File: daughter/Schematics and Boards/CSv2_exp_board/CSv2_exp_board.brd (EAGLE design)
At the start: 38.1 x 43.8 mm, 100 parts, among them J1 HIROSE-DF40_44-PIN_CONNECTORS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, J2 J-SERIAL-PORT, J3 CORTEX_DEBUG_SMD, J301 HIROSE-DF40_44-PIN_CONNECTORS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, J7 J-USB-HIROSE-MICRO-USB, SW1 SPST_TACT-KMR2, SW2 SPST_TACT-KMR2, U1 LOADSWITCH-MIC94164, U10 LOADSWITCH-MIC94164, U11 BMI160, U2 ADA4841-1YRJZ-R7, U205 MPL3115A2, U3 Value, U4 RFM69HCW, U5 Value, U6 Value, U7 LOADSWITCH-MIC94164, U8 LOADSWITCH-MIC94164, U9 LOADSWITCH-MIC94164, X1 32.768kHz, X2 32.768, X4 uFL

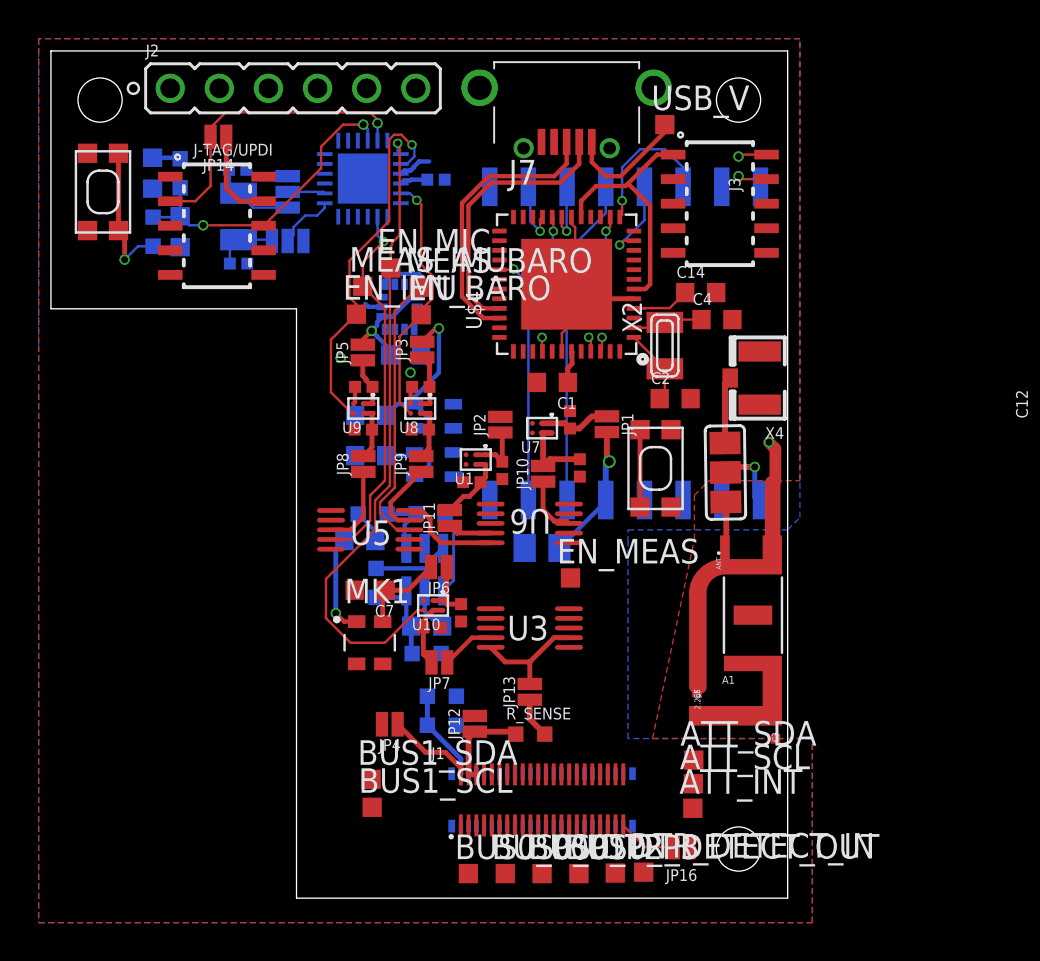
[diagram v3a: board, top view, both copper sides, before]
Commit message: DTR-routing 100% + DRC resolved
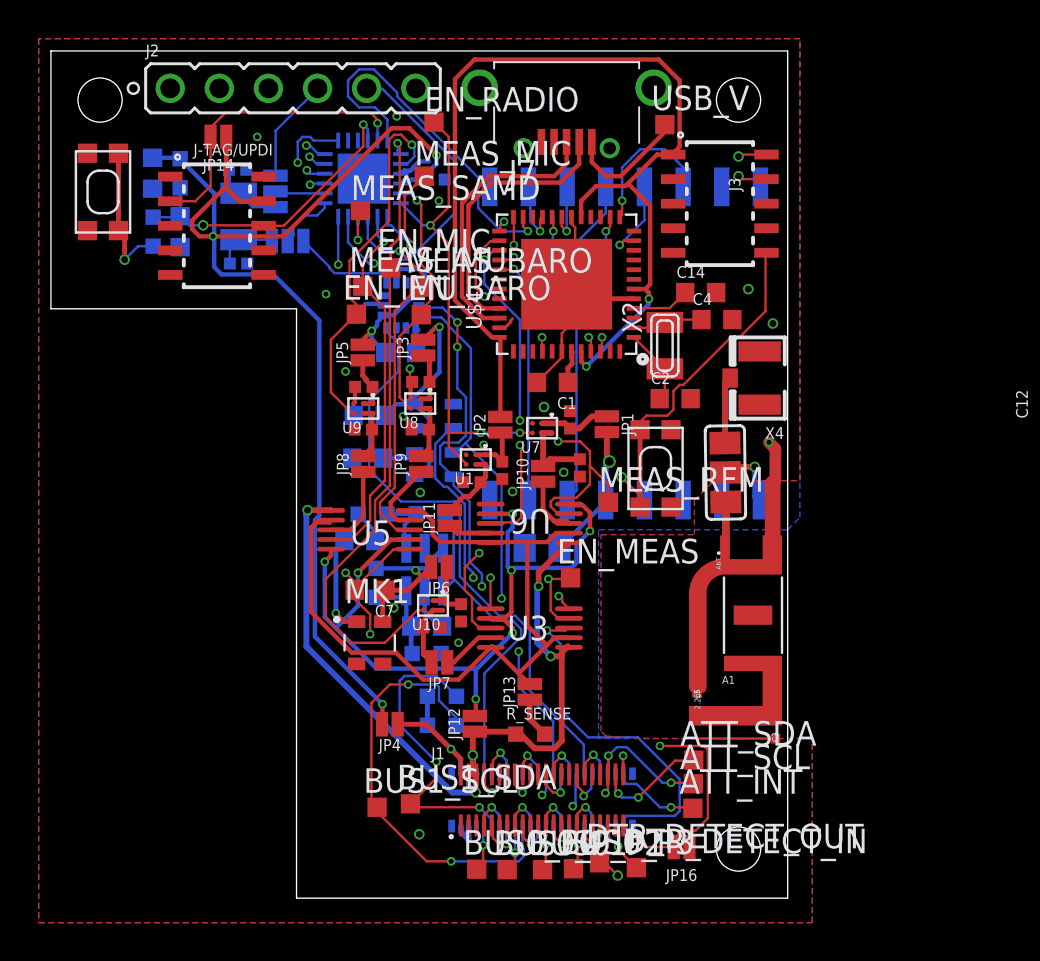
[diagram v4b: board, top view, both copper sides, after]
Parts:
- added EN_RADIO, MEAS_MIC, MEAS_RFM, MEAS_SAMD: TPTP10SQ, TestPoints:TP10SQ
- moved BUS1_SDA 2.40 mm to (18.6, 4.88)
- moved DTR_DETECT_OUT 0.97 mm to (28.4, 1.83)
- moved SJ2 0.64 mm to (11.6, 36.6)
- moved BUS0_P0 0.49 mm to (22.0, 1.50)
- moved DTR_DETECT_IN 0.44 mm to (30.3, 1.57)
- moved BUS0_P3 0.38 mm to (27.0, 1.52)
- moved C25 0.28 mm to (18.1, 28.2)
- moved BUS1_SCL 0.25 mm to (16.9, 4.70)
- moved U8 0.25 mm to (19.1, 25.6)
- moved C20 0.25 mm to (19.1, 26.7)
- moved BUS0_P1 0.23 mm to (23.6, 1.47)
- moved BUS0_P2 0.20 mm to (25.4, 1.47)
- moved C204 0.20 mm to (16.4, 22.8)
- moved JP3 0.11 mm to (19.3, 28.5)
- moved U11 0.11 mm to (18.1, 30.7)
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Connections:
- net EN_RADIO: now also EN_RADIO.TP
- net MEAS_MIC: now also MEAS_MIC.TP
- net MEAS_RFM: now also MEAS_RFM.TP
- net MEAS_SAMD: now also MEAS_SAMD.TP
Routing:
- net BUS0_GPIO0: track 0.00 -> 67.5 mm, vias 0 -> 3
- net +3V3_ATT: track 7.75 -> 63.2 mm, vias 0 -> 3
- net DTR_DETECT_OUT: track 0.00 -> 54.1 mm, vias 0 -> 2
- net DTR_DETECT_IN: track 0.00 -> 52.0 mm, vias 0 -> 2
- net BUS0_SERCOM_P0: track 0.00 -> 50.8 mm, vias 0 -> 2
- net MASTER_I2C_SCL: track 0.00 -> 50.4 mm, vias 0 -> 4
- net MASTER_I2C_SDA: track 0.00 -> 47.8 mm, vias 0 -> 3
- net BUS1_SERCOM_P1: track 0.00 -> 47.3 mm, vias 0 -> 5
- net ATT_INT: track 0.00 -> 45.9 mm, vias 0 -> 3
- net BUS0_GPIO1: track 0.00 -> 44.2 mm, vias 0 -> 2
- net BUS1_SERCOM_P0: track 0.00 -> 44.2 mm, vias 0 -> 3
- net BUS0_SERCOM_P2: track 0.00 -> 44.1 mm, vias 0 -> 3
- net BUS0_SERCOM_P1: track 0.00 -> 43.4 mm, vias 0 -> 2
- net BUS0_SERCOM_P3: track 0.00 -> 42.5 mm, vias 0 -> 2
- net +3V3_SAMD: track 13.2 -> 54.6 mm, vias 0 -> 2
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- added copper zone on layer 15, net GND
- added copper zone on layer 2, net GND

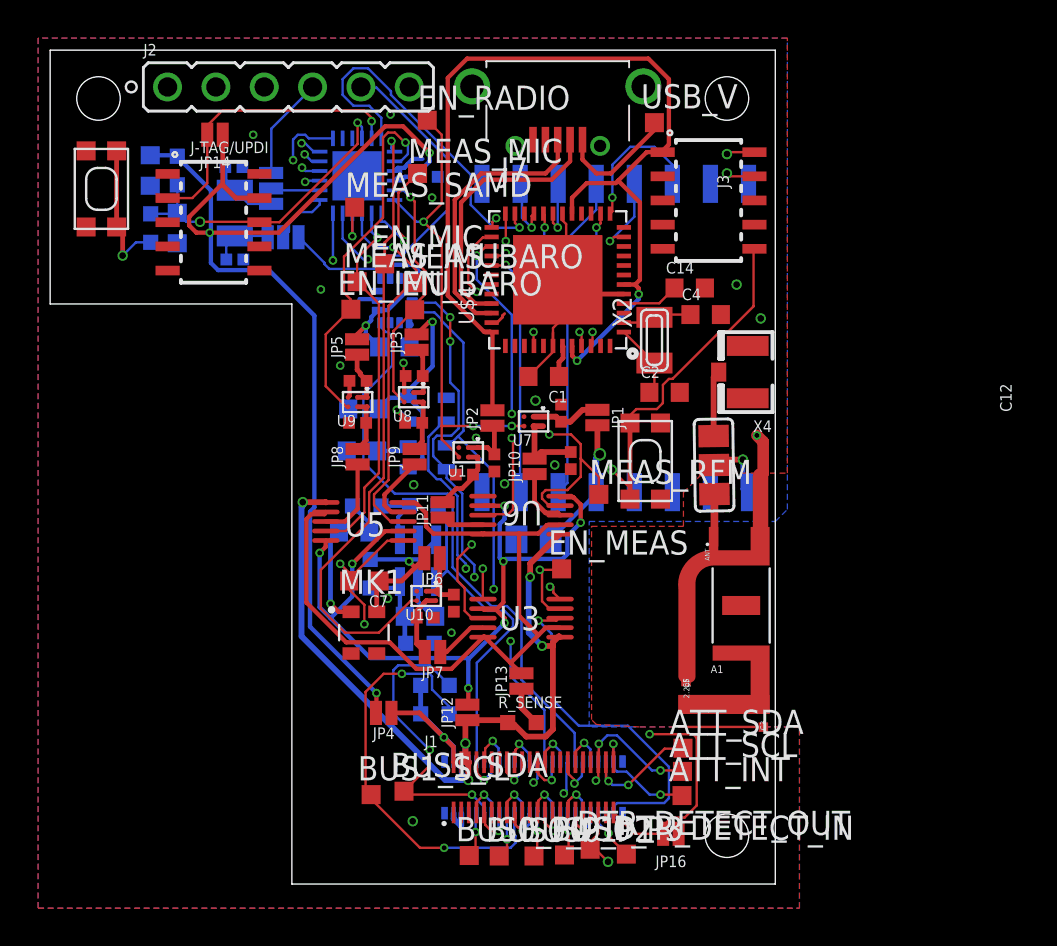
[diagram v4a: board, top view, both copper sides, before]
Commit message: DTR-added text/labels
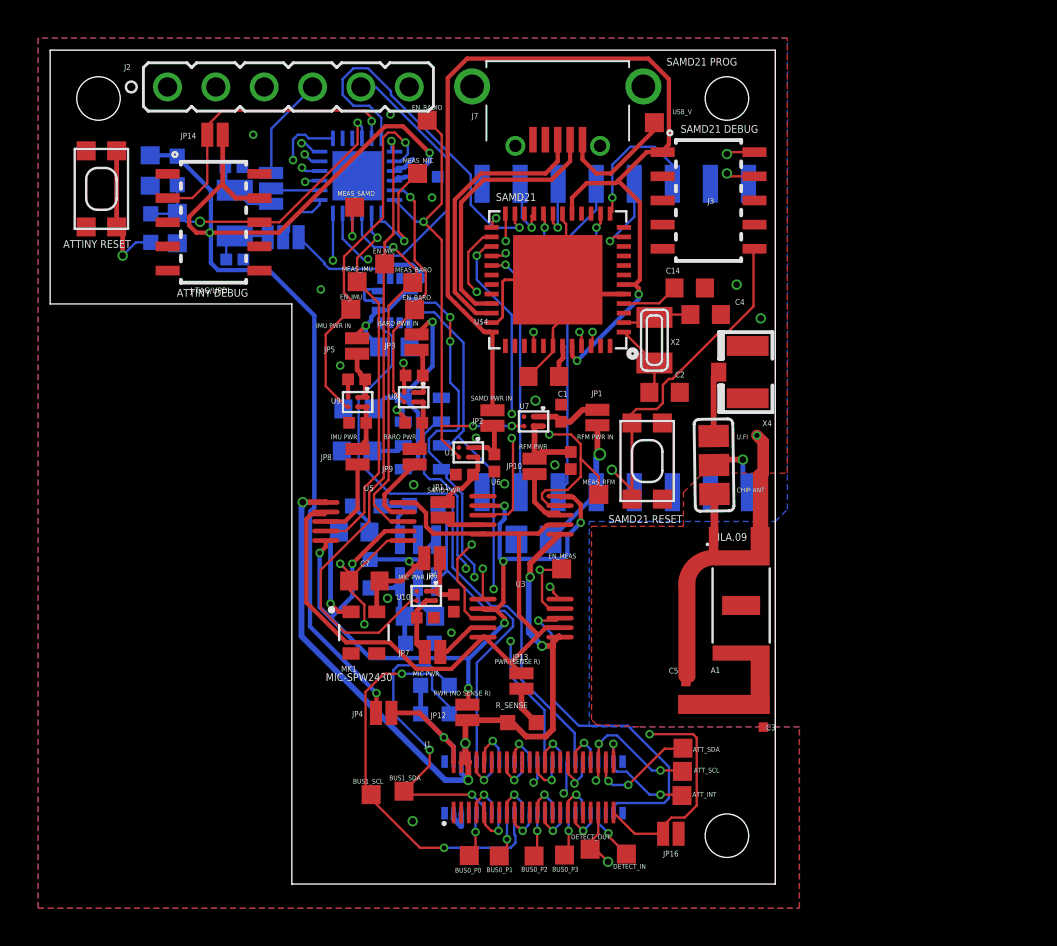
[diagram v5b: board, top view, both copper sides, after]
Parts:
- moved U205 0.25 mm to (19.6, 23.7)
- moved C203 0.25 mm to (16.2, 25.0)
- moved C204 0.25 mm to (16.1, 22.8)
- moved C22 0.11 mm to (16.1, 26.5)
- moved SW2 0.10 mm to (31.4, 22.2)
- moved JP5 0.05 mm to (16.1, 28.3)
- renumbered DTR_DETECT_IN to DETECT_IN, DTR_DETECT_OUT to DETECT_OUT
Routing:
- net GND: track 66.2 -> 62.3 mm
- net BUS1_SERCOM_P1: track 47.3 -> 47.9 mm
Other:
- board text added: "ATTINY DEBUG"
- board text added: "ATTINY RESET"
- board text added: "ATTINY-817"
- board text added: "BARO PWR"
- board text added: "BARO PWR IN"
- board text added: "CHIP ANT"
- board text added: "ILA.09"
- board text added: "IMU PWR"
- board text added: "IMU PWR IN"
- board text added: "IMU-BMI160"
- board text added: "MIC PWR"
- board text added: "MIC PWR IN"
- board text added: "MIC-SPW2430"
- board text added: "MPL3115"
- board text added: "PWR (NO SENSE R)"
- board text added: "PWR (SENSE R)"
- board text added: "RFM PWR"
- board text added: "RFM PWR IN"
- board text added: "SAMD PWR"
- board text added: "SAMD PWR IN"
- board text added: "SAMD21"
- board text added: "SAMD21 DEBUG"
- board text added: "SAMD21 PROG"
- board text added: "SAMD21 RESET"
- board text added: "U.Fl"

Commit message: DTR-added three ufl connectors for rf calibratiion
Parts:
- added R7: (no value), Resistors:R0603
- added X3, X5, X6: uFL, Connectors:U.FL
- moved SW1 1.02 mm to (2.69, 35.5)
- moved J3 0.51 mm to (34.6, 35.4)
- moved JP16 0.49 mm to (32.1, 2.59)
- moved ATT_INT 0.33 mm to (32.9, 4.85)
- moved ATT_SDA 0.30 mm to (32.9, 7.14)
- moved ATT_SCL 0.29 mm to (32.9, 5.99)
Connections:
- new net N$11: R7.1, X6.3
- net GND: now also R7.2, X3.1, X3.2, X5.1, X5.2, X5.3, X6.1, X6.2
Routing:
- net GND: track 62.3 -> 71.0 mm
- net N$11: track 0.00 -> 3.52 mm
- net LORA_RST: track 7.55 -> 6.69 mm
- net N$12: track 8.18 -> 7.46 mm
- net LORA_SCK: track 6.26 -> 5.61 mm
- net SAMD_!RESET: track 28.6 -> 28.1 mm
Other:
- outline, holes or cut-outs redrawn

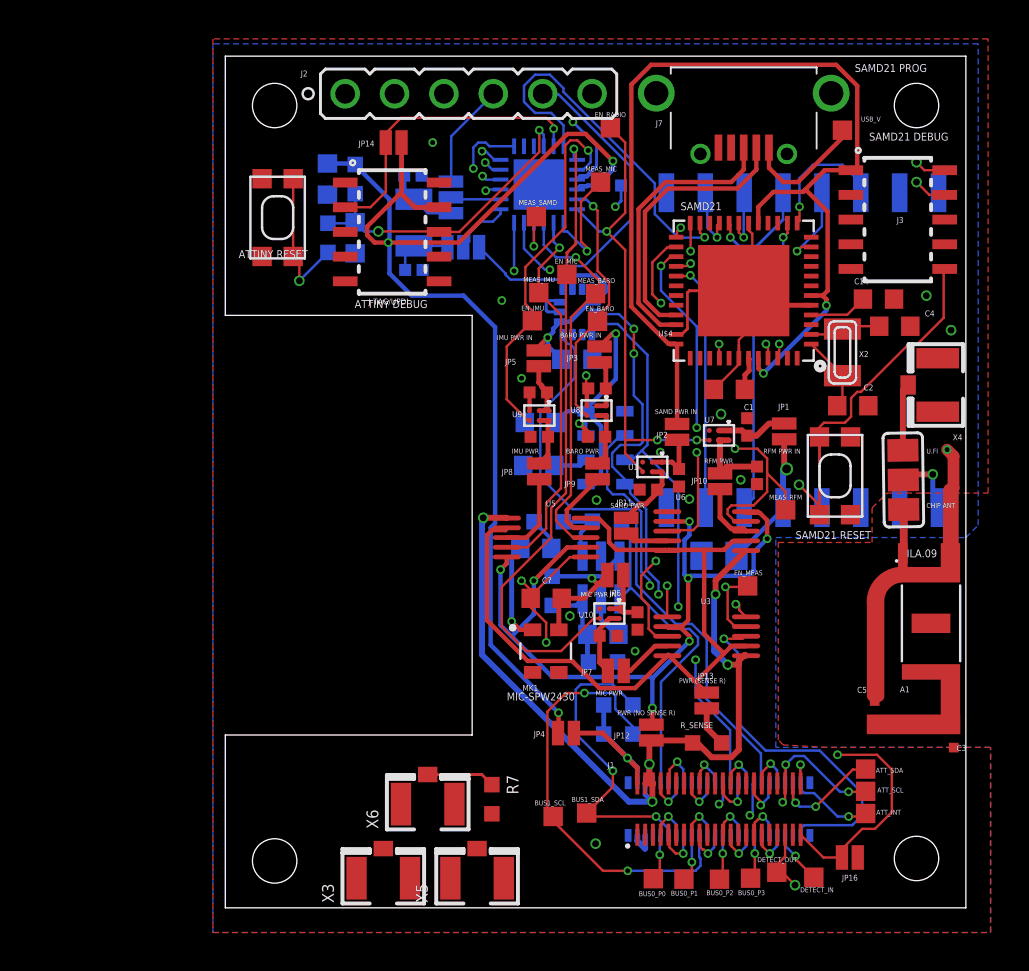
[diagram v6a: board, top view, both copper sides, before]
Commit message: DTR-added codec datasheet and did replacement
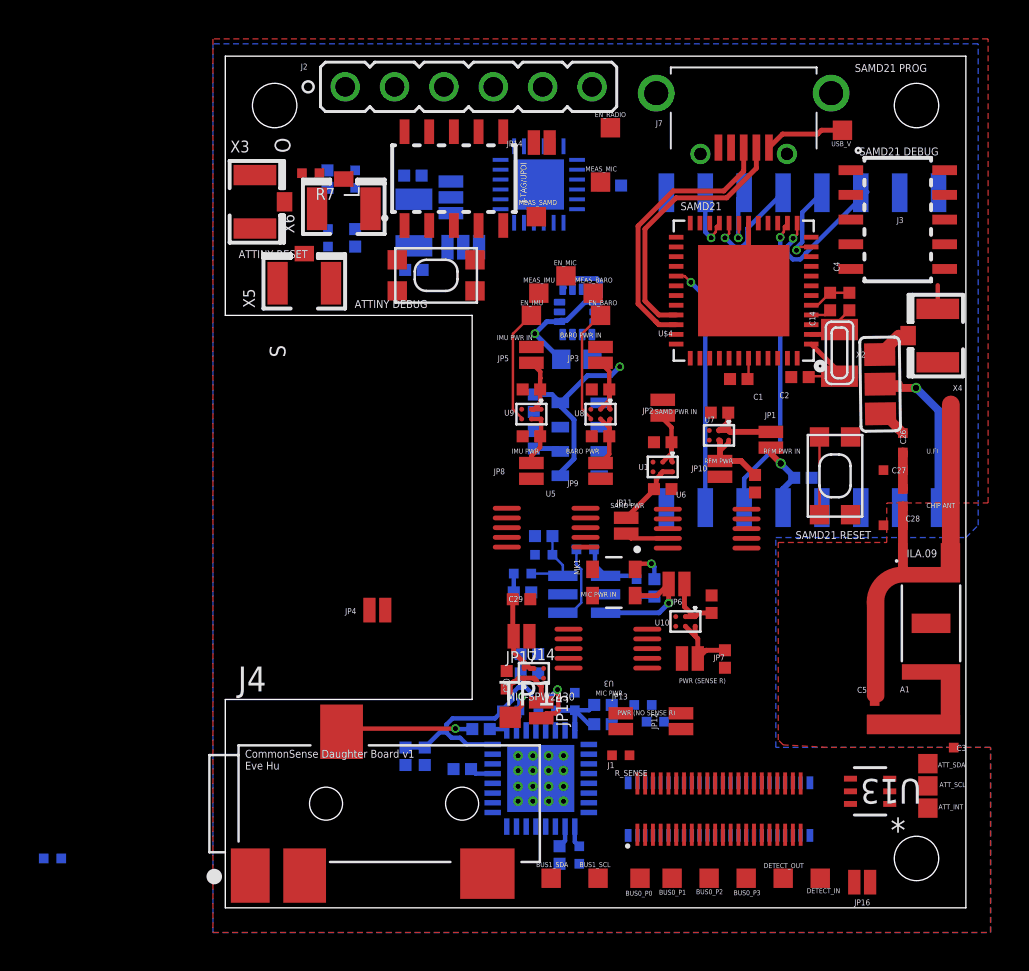
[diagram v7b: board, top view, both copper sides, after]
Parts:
- removed EN_MEAS, MEAS_RFM: TPTP10SQ, TestPoints:TP10SQ
- added C26, C27, C28: (no value), CommonSense-DTR-v1:C0402-S
- added C29: 1u, Capacitors:C0402
- added C30: 100n, Capacitors:C0402
- added C31, C32, C33: (no value), Capacitors:C0402
- added C34, C36, C38: 0.1u, Capacitors:C0402
- added C35, C37, C39: 10u, Capacitors:C0402
- added J4: SJ-43514-SMT, CommonSense-DTR-v1:CUI_SJ-43514-SMT
- added JP15, JP17: JUMPER-SMT_2_NC_PASTELG_NO-SILK, Connectors:SMT-JUMPER_2_NC_PASTE_NO-SILK
- added L1: L0402, Inductors:L0402
- added R10, R11, R9: 100k, Resistors:R0402
- added R12, R8: (no value), Resistors:R0402
- added TP1: TPTP11SQ, TestPoints:TP11SQ
- added U12: TLV320DAC26IRHB, CommonSense-DTR-v1:RHB32_3P45X3P45
- added U13: ADG839YKSZ-500RL7KS_6_ADI-L, CommonSense-DTR-v1:KS_6_ADI-L
- added U14: LOADSWITCH-MIC94164, Switches:WLCSP6_2X3
- C1, C12, C14, C2, C203, C204, C3-4.7N, C4, C6, C7, C8: device Capacitors:C0603 -> Capacitors:C0402
- C9: device Capacitors:C0805 -> Capacitors:C0402
- R1, R1-100K, R2, R3, R3-39R, R4, R5, R6, R7, R_SENSE: device Resistors:R0603 -> Resistors:R0402
- moved X3 35.4 mm to (1.52, 36.3), turned to 0 degrees
- moved R7 33.5 mm to (4.39, 37.8), turned to 180 degrees
- moved X5 31.9 mm to (4.06, 32.1)
- moved X6 30.9 mm to (6.10, 36.0)
- moved JP4 11.6 mm to (7.82, 15.3)
- moved SW1 8.68 mm to (10.8, 32.5), turned to 180 degrees
- moved JP14 7.62 mm to (16.3, 39.4)
- moved C6 6.43 mm to (22.1, 16.5), turned to 270 degrees
- moved R3 6.30 mm to (16.4, 18.2), turned to 0 degrees
- moved C23 6.11 mm to (25.7, 12.8), turned to 270 degrees
- moved C8 5.90 mm to (16.4, 19.1), turned to 0 degrees
- moved C9 5.89 mm to (29.7, 22.1), turned to 180 degrees
- moved R1 5.66 mm to (21.2, 16.5), turned to 270 degrees
- moved U3 5.12 mm to (19.7, 13.3), turned to 0 degrees
- moved SJ3 5.07 mm to (33.7, 26.9)
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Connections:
- new net +3V3_CODEC: C34.1, C35.1, C36.1, C37.1, JP15.2, R11.2, R9.2, U12.2, U12.20, U12.24
- new net +3V3_CODEC_IN: C29.1, JP17.2, U14.A2, U14.B2
- new net +3V3_CODEC_OUT: C30.1, JP15.1, U14.A1, U14.B1
- new net +3V3_CODEC_PWR: JP17.1, U3.3
- new net AGND: C31.2, C36.2, C37.2, J4.2, J4.4, R12.1, U12.15, U12.22
- new net CODEC_!RESET: R11.1, TP1.TP, U12.26
- new net EN_CODEC: ATTINY-817.21, U14.C2
- new net MEAS_CODEC: ATTINY-817.20, U3.4
- new net N$13: C26.2, C27.1, L1.1
- new net N$14: R8.1, U12.9
- new net N$15: C31.1, U12.21
- new net N$16: C32.2, J4.3
- new net N$21: C38.1, C39.1, R10.1, R9.1, U12.32
- new net N$25: C32.1, U12.25
- new net N$27: C33.1, U12.10
- new net N$28: C33.2, J4.1, R8.2
- new net N$9: C26.1, SJ3.1
- new net VGND: U12.23
- net +3V3_DTR: now also U13.2
- net +3V3_MEAS: now also U13.6
- net +3V3_NMEAS: now also U3.5
- net BUS0_AIN0: now also ATTINY-817.24; no longer R2.1, U2.1
- net BUS0_GPIO0: now also U$4.24; no longer ATTINY-817.24, U$4.23
- net BUS0_GPIO1: now also U12.7; no longer U$4.24
- net BUS0_SERCOM_P0: now also U12.5
- net BUS0_SERCOM_P1: now also U12.4
- net BUS0_SERCOM_P3: now also U12.6
- net BUS1_AIN0: now also R2.1, U2.1
- net EN_MEAS: now also U13.1; no longer EN_MEAS.TP, U3.4
- net GND: now also C27.2, C28.1, C28.2, C29.2, C30.2, C34.2, C35.2, C38.2, C39.2, L1.2, R10.2, R12.2, U12.1, U13.3, U14.C1; no longer SJ3.1
- net MEAS_RFM: no longer MEAS_RFM.TP
- net V_SENSE_IN: now also U13.4; no longer U3.5
- net V_SENSE_OUT: now also U13.5; no longer U3.3
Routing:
- net BUS0_GPIO0: track 67.5 -> 0.00 mm, vias 3 -> 0
- net +3V3_ATT: track 63.2 -> 0.00 mm, vias 3 -> 0
- net +3V3_SAMD: track 55.1 -> 0.00 mm, vias 2 -> 0
- net DTR_DETECT_OUT: track 54.1 -> 0.00 mm, vias 2 -> 0
- net DTR_DETECT_IN: track 52.0 -> 0.00 mm, vias 2 -> 0
- net BUS0_SERCOM_P0: track 50.8 -> 0.00 mm, vias 2 -> 0
- net MASTER_I2C_SCL: track 50.1 -> 0.00 mm, vias 4 -> 0
- net BUS1_SERCOM_P1: track 47.9 -> 0.00 mm, vias 5 -> 0
- net MASTER_I2C_SDA: track 47.5 -> 0.00 mm, vias 3 -> 0
- net ATT_INT: track 45.7 -> 0.00 mm, vias 3 -> 0
- net GND: track 71.0 -> 26.5 mm, vias 20 -> 0
- net BUS1_SERCOM_P0: track 44.4 -> 0.00 mm, vias 3 -> 0
- net BUS0_GPIO1: track 44.2 -> 0.00 mm, vias 2 -> 0
- net BUS0_SERCOM_P2: track 44.1 -> 0.00 mm, vias 3 -> 0
- net +3V3_DTR: track 43.6 -> 0.00 mm, vias 5 -> 0
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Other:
- outline, holes or cut-outs redrawn
- board text added: "CommonSense Daughter Board v1 Eve Hu"
- board text added: "L"
- board text added: "O"
- board text added: "S"
